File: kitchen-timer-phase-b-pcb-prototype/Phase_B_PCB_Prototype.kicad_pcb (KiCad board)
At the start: 2 copper layers, 99.1 x 99.1 mm, 47 parts, among them J1 USB_B_Mini, J2 AVR-ISP-6, J3 ESP Connector, U1 CA56-12EWA, U2 74HC595, U3 ATmega32U4-A, U4 USBLC6-2SC6, U5 LP2985-3.3, Y1 Crystal_GND24

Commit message: Progressing on PCB layout
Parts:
- moved J3 88.0 mm to (73.7, 50.0)
- moved J1 86.9 mm to (158.5, 113.0)
- moved R15 86.9 mm to (159.1, 106.9)
- moved R16 86.9 mm to (157.2, 106.9)
- moved U4 86.9 mm to (158.0, 101.5)
- moved J2 84.6 mm to (161.8, 72.4)
- moved D1 82.8 mm to (85.9, 92.2)
- moved R17 82.2 mm to (72.1, 65.3)
- moved R3 80.3 mm to (90.5, 95.2)
- moved D3 72.4 mm to (150.9, 113.1)
- moved R1 59.5 mm to (99.8, 106.8)
- moved S1 59.5 mm to (89.7, 104.9)
- moved C9 54.7 mm to (137.8, 108.8)
- moved C1 54.7 mm to (152.2, 94.0)
- moved C3 54.7 mm to (132.8, 109.0)
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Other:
- board size 99.1 x 99.1 mm -> 99.1 x 75.4 mm

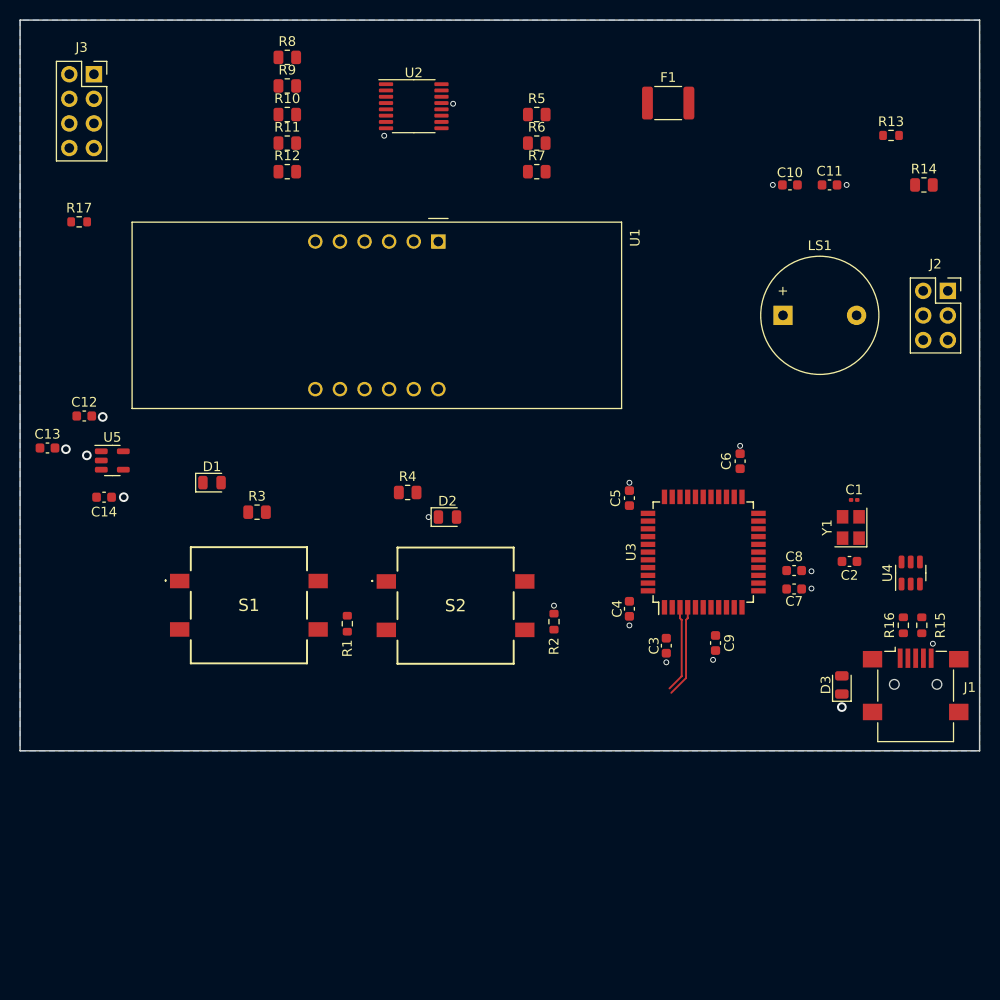
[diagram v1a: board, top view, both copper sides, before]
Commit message: PCB layout and routing
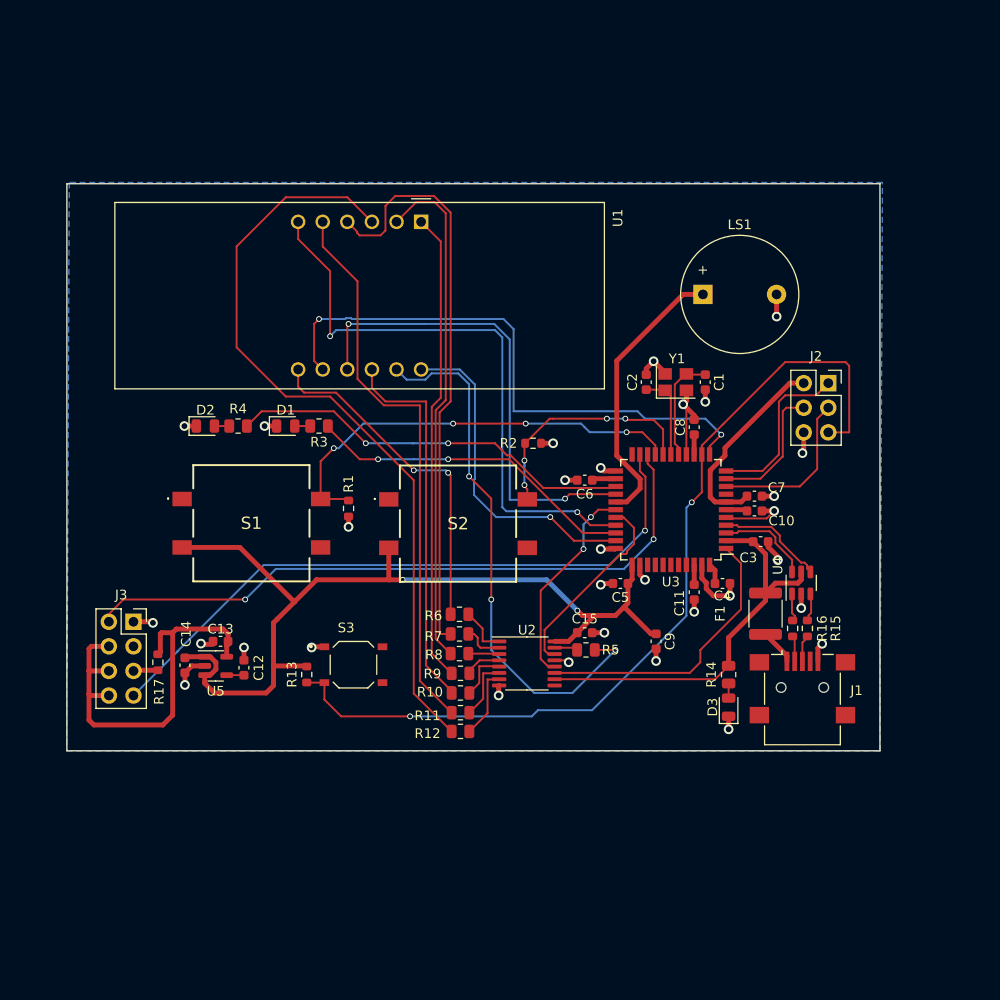
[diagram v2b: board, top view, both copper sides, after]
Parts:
- added C15: 0.1u, Capacitor_SMD:C_0603_1608Metric, F.Cu at (124.3, 107.7)
- added S3: PTS526_SM08_SMTR2_LFS, PTS526_SMD_Button:PTS526_SMD_Button, F.Cu at (100.5, 111.0)
- C1: footprint Capacitor_SMD:C_0201_0603Metric -> Capacitor_SMD:C_0603_1608Metric
- C11: value 0.2uF -> 0.1uF
- R14: value 330 -> 1k
- R15, R16: value 330 -> 22
- moved R13 82.1 mm to (95.6, 112.0), turned to -90 degrees
- moved R8 64.1 mm to (111.4, 109.9), turned to 180 degrees
- moved R9 63.2 mm to (111.5, 111.9), turned to 180 degrees
- moved R10 62.3 mm to (111.5, 113.9), turned to 180 degrees
- moved R11 61.5 mm to (111.5, 116.0), turned to 180 degrees
- moved R12 60.5 mm to (111.5, 117.9), turned to 180 degrees
- moved U2 58.7 mm to (118.4, 110.9)
- moved J3 56.7 mm to (77.7, 106.6)
- moved R5 55.5 mm to (124.5, 109.5)
- moved R14 54.4 mm to (139.2, 112.0), turned to -90 degrees
- moved F1 53.7 mm to (143.0, 105.7), turned to 90 degrees
- moved R6 49.3 mm to (111.4, 105.8), turned to 180 degrees
- moved R7 48.4 mm to (111.4, 107.8), turned to 180 degrees
- moved R17 46.2 mm to (80.3, 110.7), turned to -90 degrees
- moved C11 44.3 mm to (135.6, 103.5), turned to -90 degrees
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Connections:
- C14 pad 1: RST -> +5V
- C3 pad 1: RST -> +5V
- C4 pad 1: RST -> +5V
- C5 pad 1: RST -> +5V
- C6 pad 1: RST -> +5V
- C7 pad 1: RST -> +5V
- C8 pad 1: RST -> +5V
- C9 pad 1: RST -> +5V
- F1 pad 2: RST -> +5V
- J2 pad 2: RST -> +5V
- R13 pad 1: RST -> +5V
- R14 pad 1: RST -> +5V
- S1 pad B1: unconnected-(S1-NO_2-PadB1) -> Button_1
- S1 pad C1: RST -> +5V
- S1 pad D1: Button_1 -> unconnected-(S1-COM_2-PadD1)
- S2 pad B1: unconnected-(S2-NO_2-PadB1) -> Button_2
- S2 pad C1: RST -> +5V
- S2 pad D1: Button_2 -> unconnected-(S2-COM_2-PadD1)
- U2 pad 10: RST -> +5V
- U2 pad 16: RST -> +5V
- U3 pad 14: RST -> +5V
- U3 pad 2: RST -> +5V
- U3 pad 24: RST -> +5V
- U3 pad 34: RST -> +5V
- U3 pad 44: RST -> +5V
- U3 pad 7: RST -> +5V
- U4 pad 5: RST -> +5V
- U5 pad 1: RST -> +5V
- U5 pad 3: RST -> +5V
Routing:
- net +5V: track 0.00 -> 165.3 mm, vias 0 -> 2
- net RST: track 0.00 -> 92.2 mm, vias 0 -> 2
- net Net-(U1-DPX): track 0.00 -> 79.1 mm
- net TX: track 0.00 -> 69.2 mm, vias 0 -> 2
- net GND: track 0.00 -> 68.6 mm, vias 6 -> 31
- net RX: track 0.00 -> 68.0 mm, vias 0 -> 1
- net Dig4: track 0.00 -> 61.5 mm, vias 0 -> 2
- net Net-(U1-c): track 0.00 -> 60.2 mm
- net Dig3: track 0.00 -> 59.9 mm, vias 0 -> 2
- net Net-(U1-g): track 0.00 -> 58.4 mm
- net Dig2: track 0.00 -> 57.7 mm, vias 0 -> 2
- net Net-(U1-a): track 0.00 -> 55.8 mm, vias 0 -> 3
- net Net-(U1-d): track 0.00 -> 52.9 mm
- net Net-(U1-e): track 0.00 -> 48.7 mm
- net Button_1: track 0.00 -> 44.9 mm, vias 0 -> 4
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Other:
- board size 99.1 x 75.4 mm -> 83.9 x 58.5 mm
